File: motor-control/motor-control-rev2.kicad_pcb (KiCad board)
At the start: 2 copper layers, 122.3 x 65.9 mm, 80 parts, among them P1 CONN_02X12, P2 to_motor_phase_1, P3 to_motor_phase_2, P4 to_motor_phase_3, P5 CONN_01X01, P6 CONN_01X01, P7 CONN_01X04, Q1 csd19505kcs, Q10 csd19505kcs, Q11 csd19505kcs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

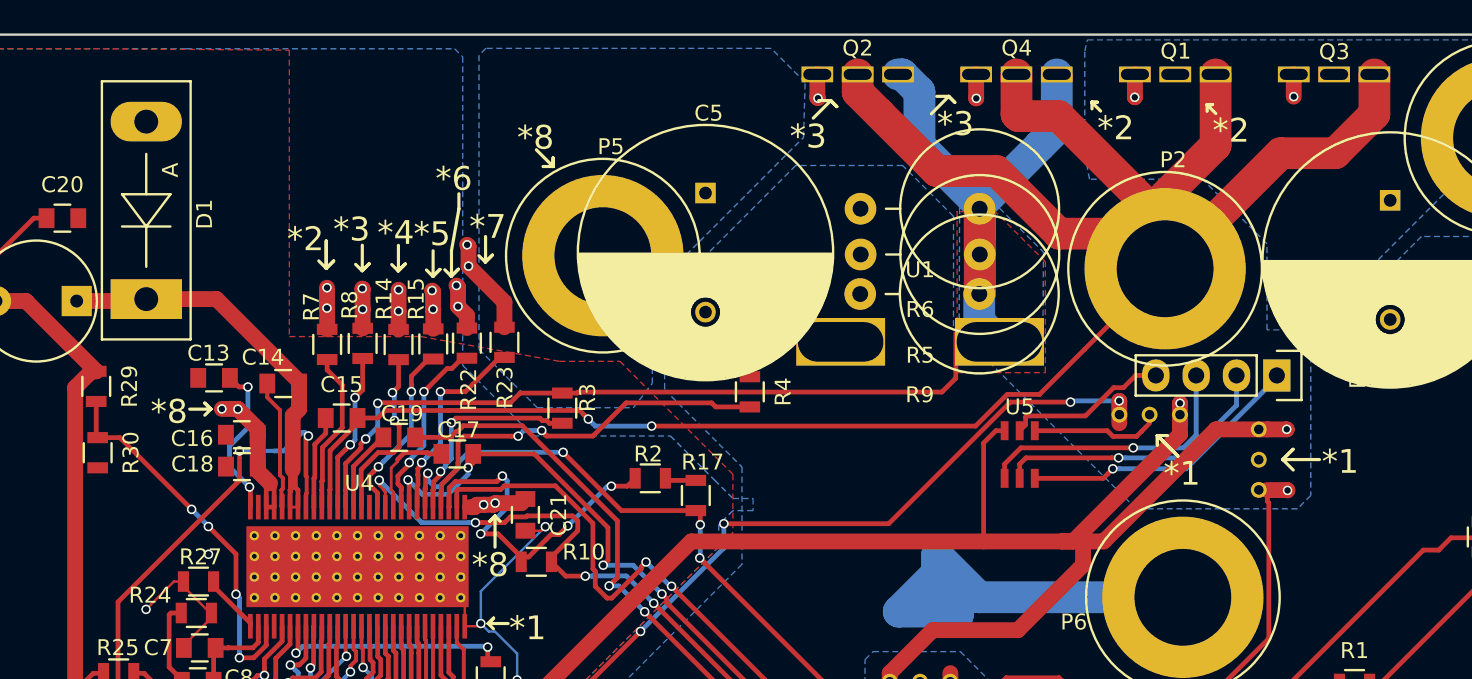
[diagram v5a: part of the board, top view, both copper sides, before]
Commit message: Connected grounds, moved temp sensor, some silk
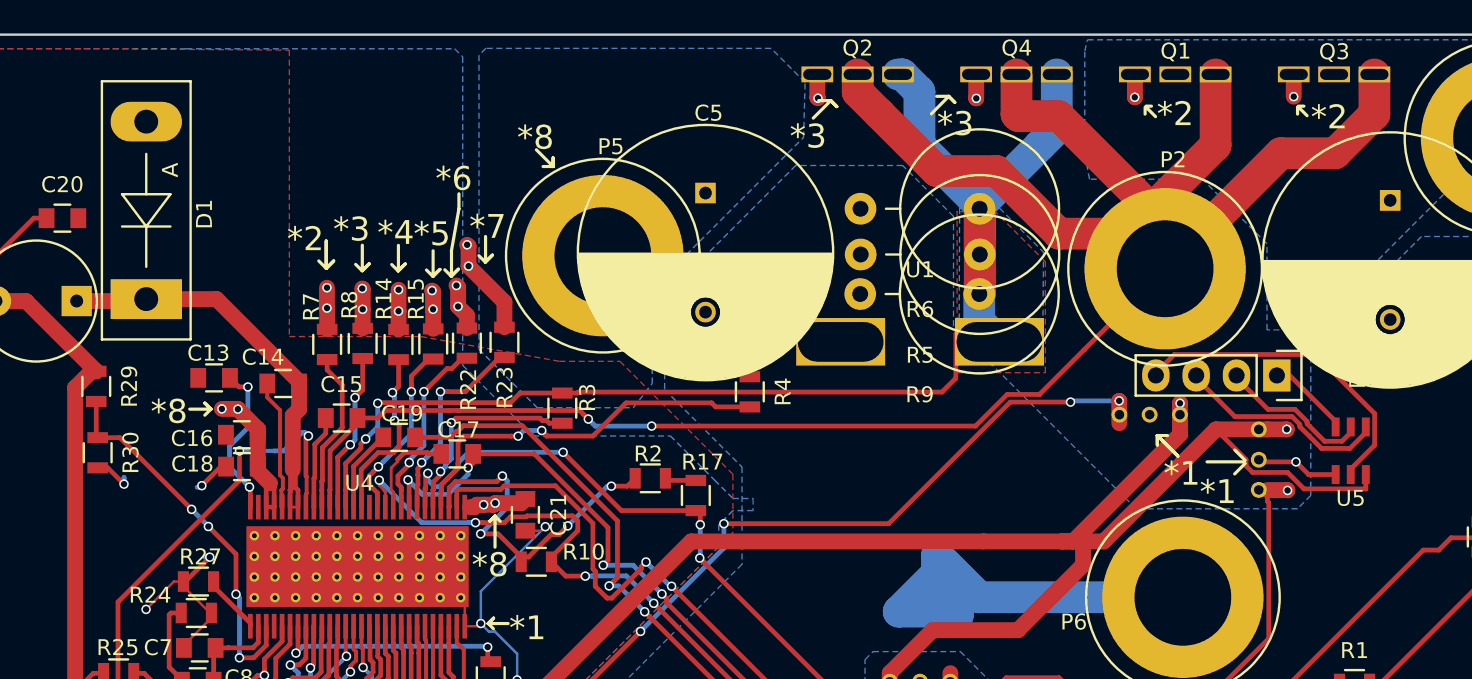
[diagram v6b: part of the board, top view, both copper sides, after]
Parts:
- moved U5 20.8 mm to (178.6, 80.7), turned to 0 degrees
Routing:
- net Net-(P7-Pad1): track 18.0 -> 5.40 mm, vias 1 -> 0
- net Net-(P7-Pad4): track 10.3 -> 20.4 mm
- net Net-(P7-Pad2): track 18.0 -> 9.66 mm, vias 1 -> 0
- net GND: track 97.1 -> 102.2 mm, vias 5 -> 9
- net VCC: track 179.6 -> 183.9 mm
- net Net-(P7-Pad3): track 17.5 -> 13.5 mm, vias 1 -> 0
- net (no net): track 0.04 -> 0.00 mm, vias 1 -> 0

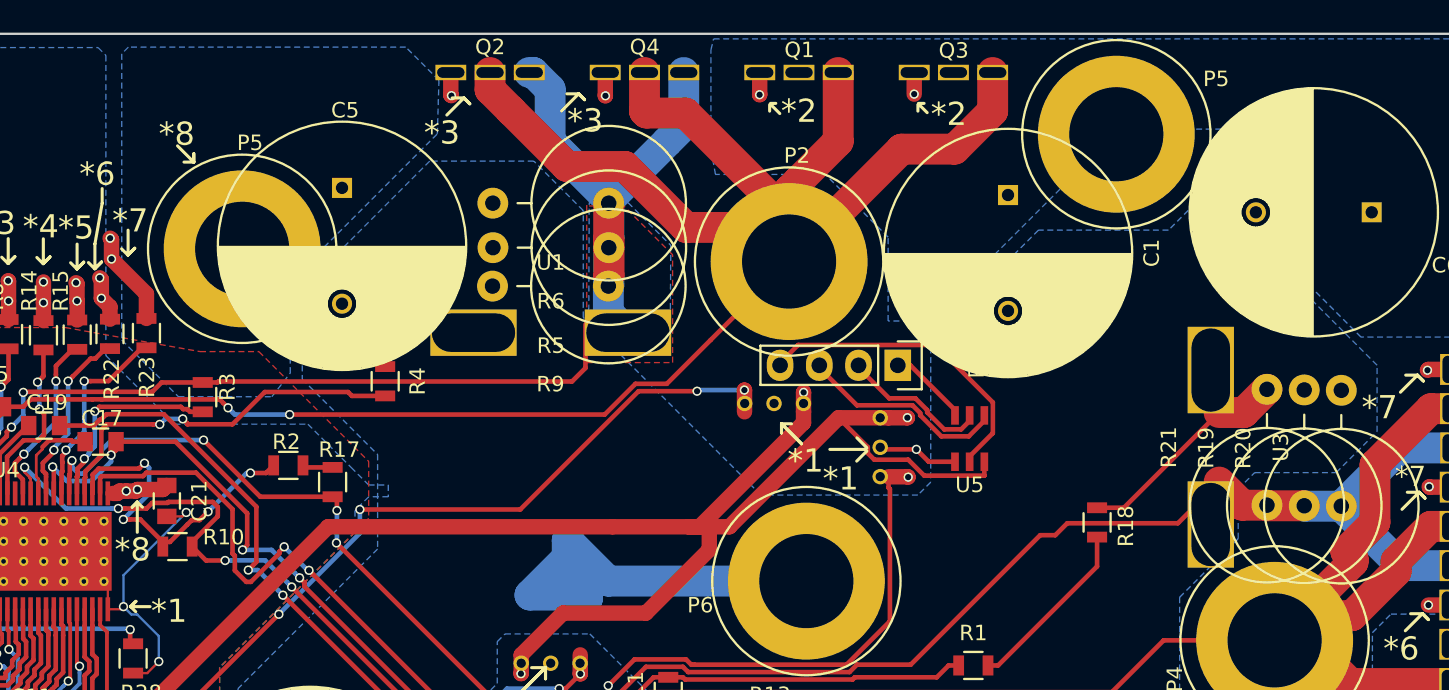
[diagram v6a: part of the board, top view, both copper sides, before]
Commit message: Moved a batt pin up left, began right hall fixes
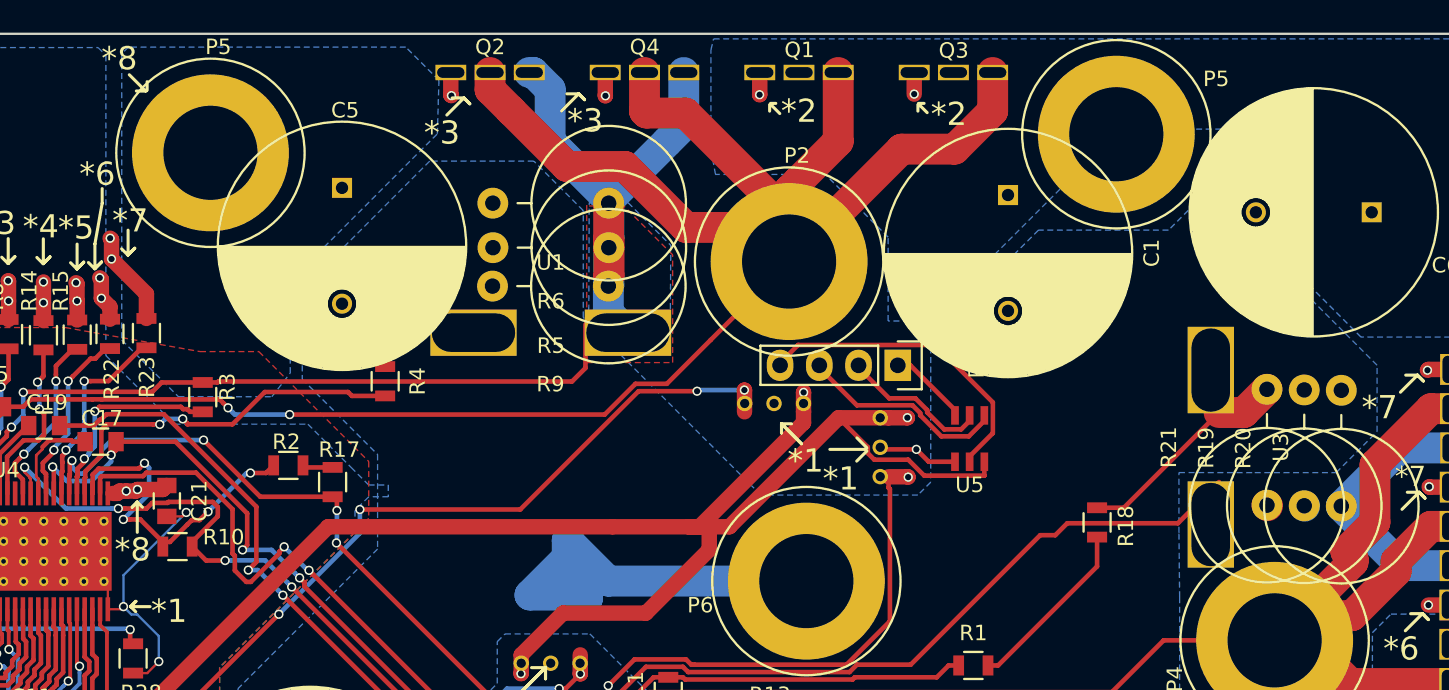
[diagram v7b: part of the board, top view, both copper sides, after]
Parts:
- moved P5 6.54 mm to (129.4, 62.2)
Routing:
- net /Gate-Driver/SL_C: track 118.3 -> 109.9 mm
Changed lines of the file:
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@@
     (area 89.8746 51.538 232.118085 134.720001)
     (thickness 1.6)
-    (drawings 144)
-    (tracks 1287)
+    (drawings 143)
+    (tracks 1283)
     (zones 0)
     (modules 80)
@@
     (36 B.SilkS user)
     (37 F.SilkS user)
-    (38 B.Mask user)
+    (38 B.Mask user hide)
     (39 F.Mask user)
     (40 Dwgs.User user)
@@
   )
   (module Connect:Banana_Jack_1Pin (layer F.Cu)
-    (at 131.4535 68.4142)
+    (at 129.4 62.2)
     (descr "Single banana socket, footprint - 6mm drill")
     (tags "banana socket")
@@
       (net 2 GND))
   )
-  (gr_text *8 (at 127.2159 60.9854) (layer F.SilkS)
+  (gr_text *8 (at 123.5 56.1) (layer F.SilkS)
     (effects (font (size 1.5 1.5) (thickness 0.3)))
   )
-  (gr_line (start 128.3208 62.8015) (end 127.6858 62.8015) (layer F.SilkS) (width 0.2))
-  (gr_line (start 128.3208 62.2554) (end 128.3208 62.8015) (layer F.SilkS) (width 0.2))
-  (gr_line (start 128.3208 62.8015) (end 128.3208 62.2554) (layer F.SilkS) (width 0.2))
-  (gr_line (start 127.2667 61.7474) (end 128.3208 62.8015) (layer F.SilkS) (width 0.2))
+  (gr_line (start 125.235 58.2) (end 124.6 58.2) (layer F.SilkS) (width 0.2))
+  (gr_line (start 125.3 57.6) (end 125.3 58.1461) (layer F.SilkS) (width 0.2))
+  (gr_line (start 124.1459 57.1459) (end 125.2 58.2) (layer F.SilkS) (width 0.2))
   (gr_text *8 (at 104.14 78.2447) (layer F.SilkS)
     (effects (font (size 1.5 1.5) (thickness 0.3)))
@@
   (segment (start 137.5876 84.7464) (end 137.3082 84.467) (width 0.3) (layer F.Cu) (net 50))
   (via (at 137.5876 85.356) (size 0.6) (drill 0.4) (layers F.Cu B.Cu) (net 50))
-  (segment (start 197.7983 85.0131) (end 196.1981 85.0131) (width 2) (layer F.Cu) (net 50))
-  (segment (start 196.1981 85.0131) (end 194.6995 83.5145) (width 2) (layer F.Cu) (net 50))
-  (segment (start 200.2113 85.0512) (end 197.8364 85.0512) (width 2) (layer F.Cu) (net 50))
   (segment (start 197.8364 85.0512) (end 197.7983 85.0131) (width 2) (layer F.Cu) (net 50))
-  (segment (start 202.6116 85.0766) (end 200.2367 85.0766) (width 2) (layer B.Cu) (net 50))
   (segment (start 200.2367 85.0766) (end 200.2113 85.0512) (width 2) (layer B.Cu) (net 50))
   (segment (start 202.6116 85.0766) (end 206.4597 88.9247) (width 2) (layer B.Cu) (net 50))
@@
         (xy 175.5225 104.7743) (xy 182.66752 104.7743) (xy 185.82474 107.93152) (xy 190.0513 107.93152) (xy 194.03656 111.91678)
         (xy 197.24712 111.91678) (xy 198.89812 110.26578) (xy 198.89812 101.90664) (xy 196.2235 99.23202) (xy 194.42518 99.23202)
-        (xy 192.14426 96.9511) (xy 192.14426 90.97194) (xy 195.93394 87.18226) (xy 195.93394 83.97424) (xy 197.00328 82.9049)
+        (xy 192.14426 96.9511) (xy 192.14426 90.97194) (xy 192.1 86.8) (xy 192.1 82.9) (xy 197.00328 82.9049)
         (xy 202.27632 82.9049) (xy 204.92554 80.25568) (xy 204.92554 75.95292) (xy 200.06398 71.09136) (xy 200.06398 64.82264)
         (xy 196.5156 61.27426) (xy 195.25322 61.27426) (xy 194.46328 62.0642) (xy 194.46328 64.16478) (xy 191.4229 67.20516)

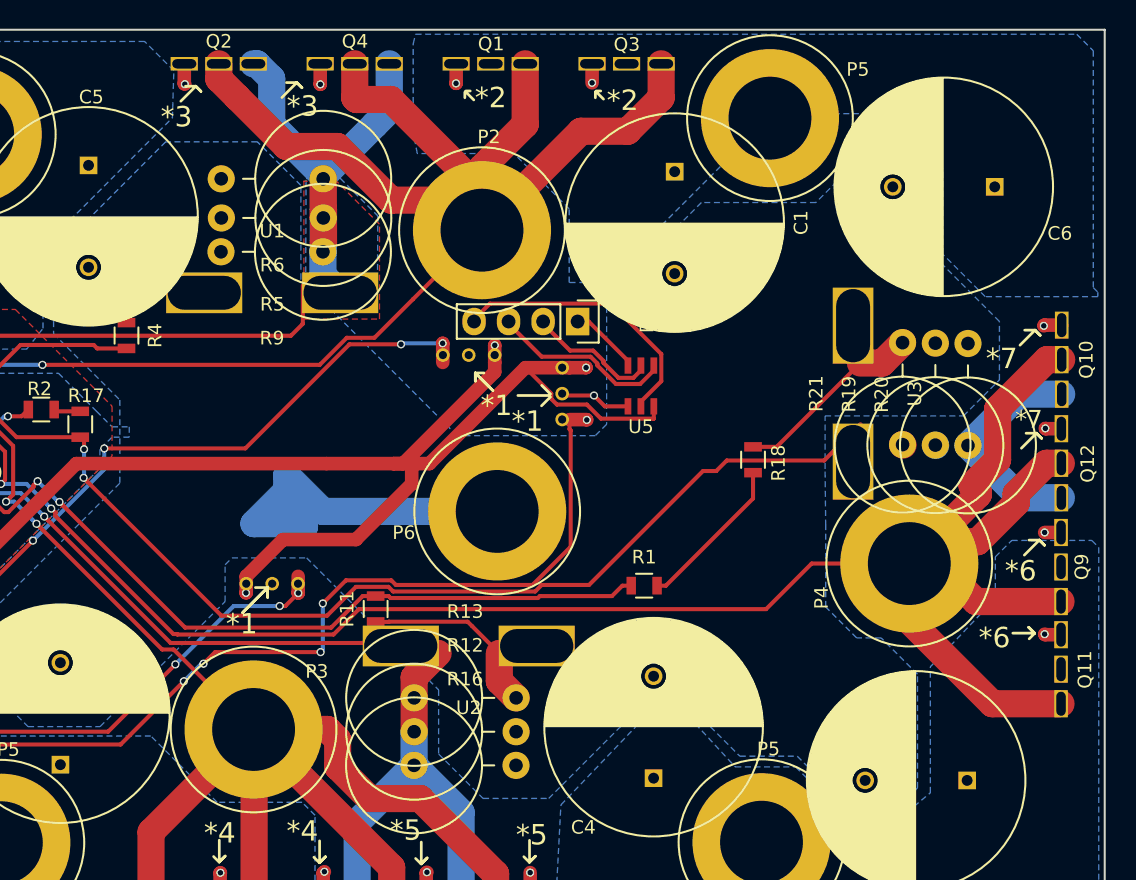
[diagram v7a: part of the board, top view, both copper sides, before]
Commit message: Finished right side mosfet separation
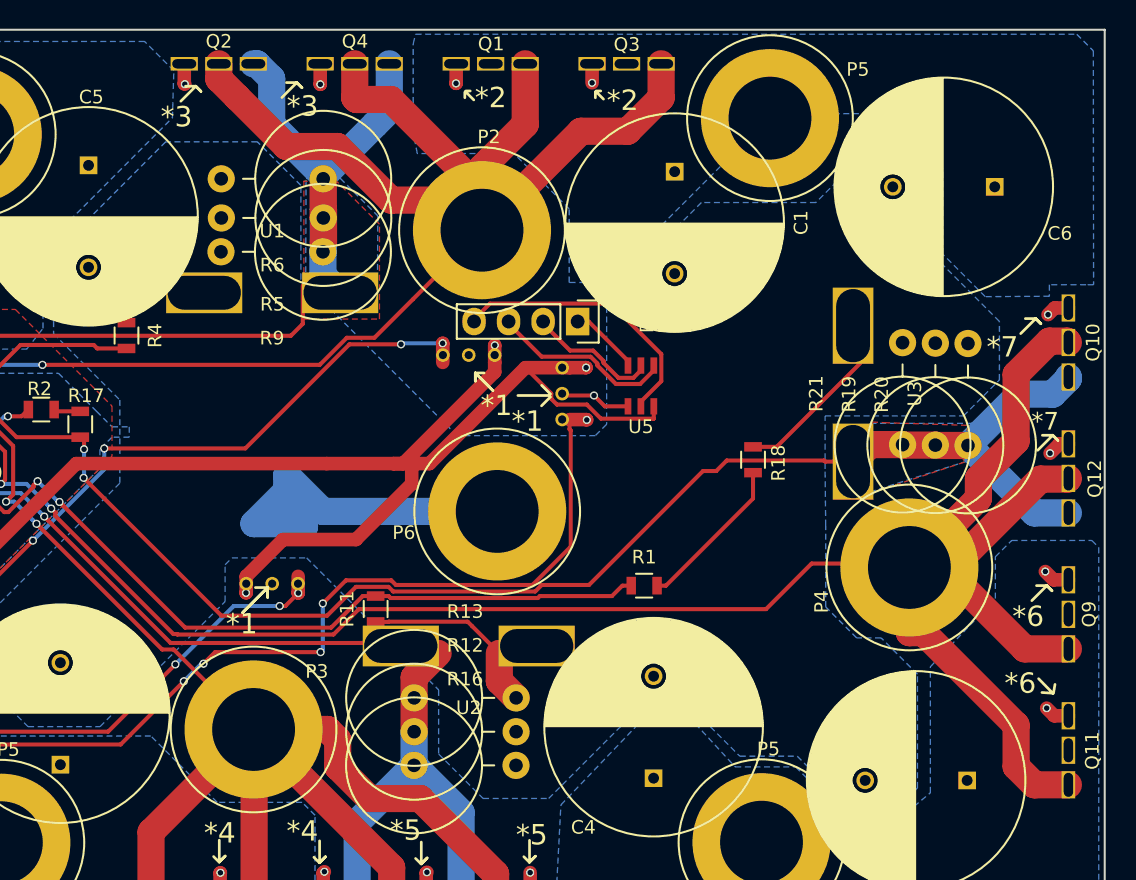
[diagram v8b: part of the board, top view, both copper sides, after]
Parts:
- moved Q11 5.99 mm to (210.0, 107.5)
- moved Q9 3.52 mm to (210.0, 97.5)
- moved Q10 1.36 mm to (210.0, 77.5)
- moved Q12 1.23 mm to (210.0, 87.5)
- moved P4 0.29 mm to (198.3, 94.0)
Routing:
- net /Gate-Driver/SH_C: track 164.0 -> 180.9 mm
- net /Gate-Driver/SL_C: track 109.9 -> 119.3 mm
- net GND: track 102.2 -> 98.5 mm
- net Net-(Q11-Pad1): track 5.38 -> 6.74 mm
- net Net-(Q10-Pad1): track 8.70 -> 9.51 mm
- added copper zone on B.Cu, net /Gate-Driver/SL_C
- added copper zone on F.Cu, net /Gate-Driver/SL_C
